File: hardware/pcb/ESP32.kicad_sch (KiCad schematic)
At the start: 8 parts, among them SW1 BOOT, U1 ESP32-WROOM-32

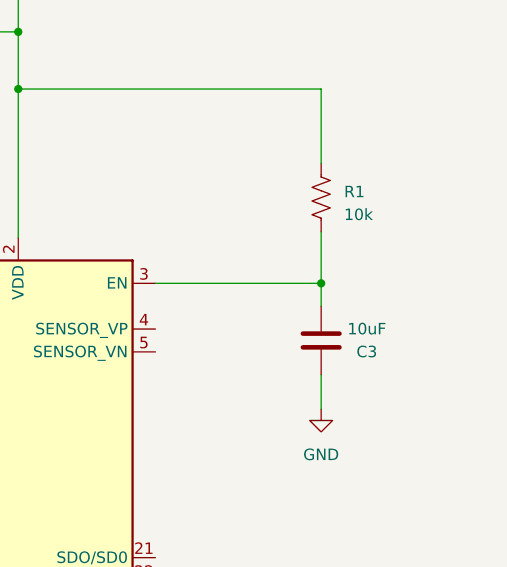
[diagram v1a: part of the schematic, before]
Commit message: Break out ESP enable pin
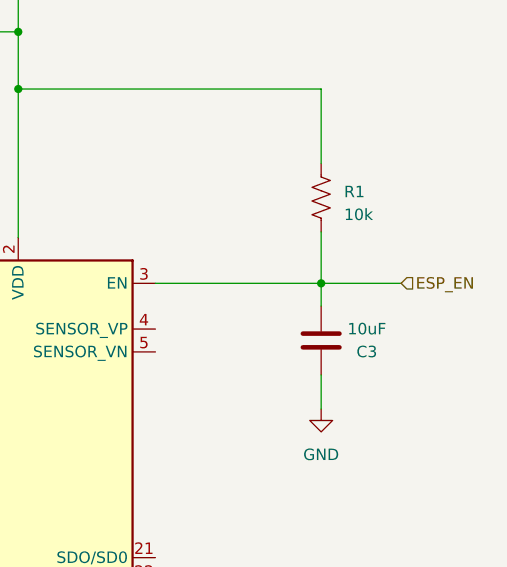
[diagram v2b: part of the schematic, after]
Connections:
- net ESP_EN: now reaches C3.2, R1.1, U1.3 (EN)
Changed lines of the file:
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@@
+    (stroke (width 0) (type default))
+  )
+  (wire (pts (xy 188.595 70.485) (xy 197.485 70.485))
     (stroke (width 0) (type default))
   )
@@
     (effects (font (size 1.27 1.27)) (justify right))
   )
+  (hierarchical_label "ESP_EN" (shape input) (at 197.485 70.485 0) (fields_autoplaced)
+    (effects (font (size 1.27 1.27)) (justify left))
+  )
   (hierarchical_label "ESP_TX" (shape input) (at 121.92 73.025 180) (fields_autoplaced)

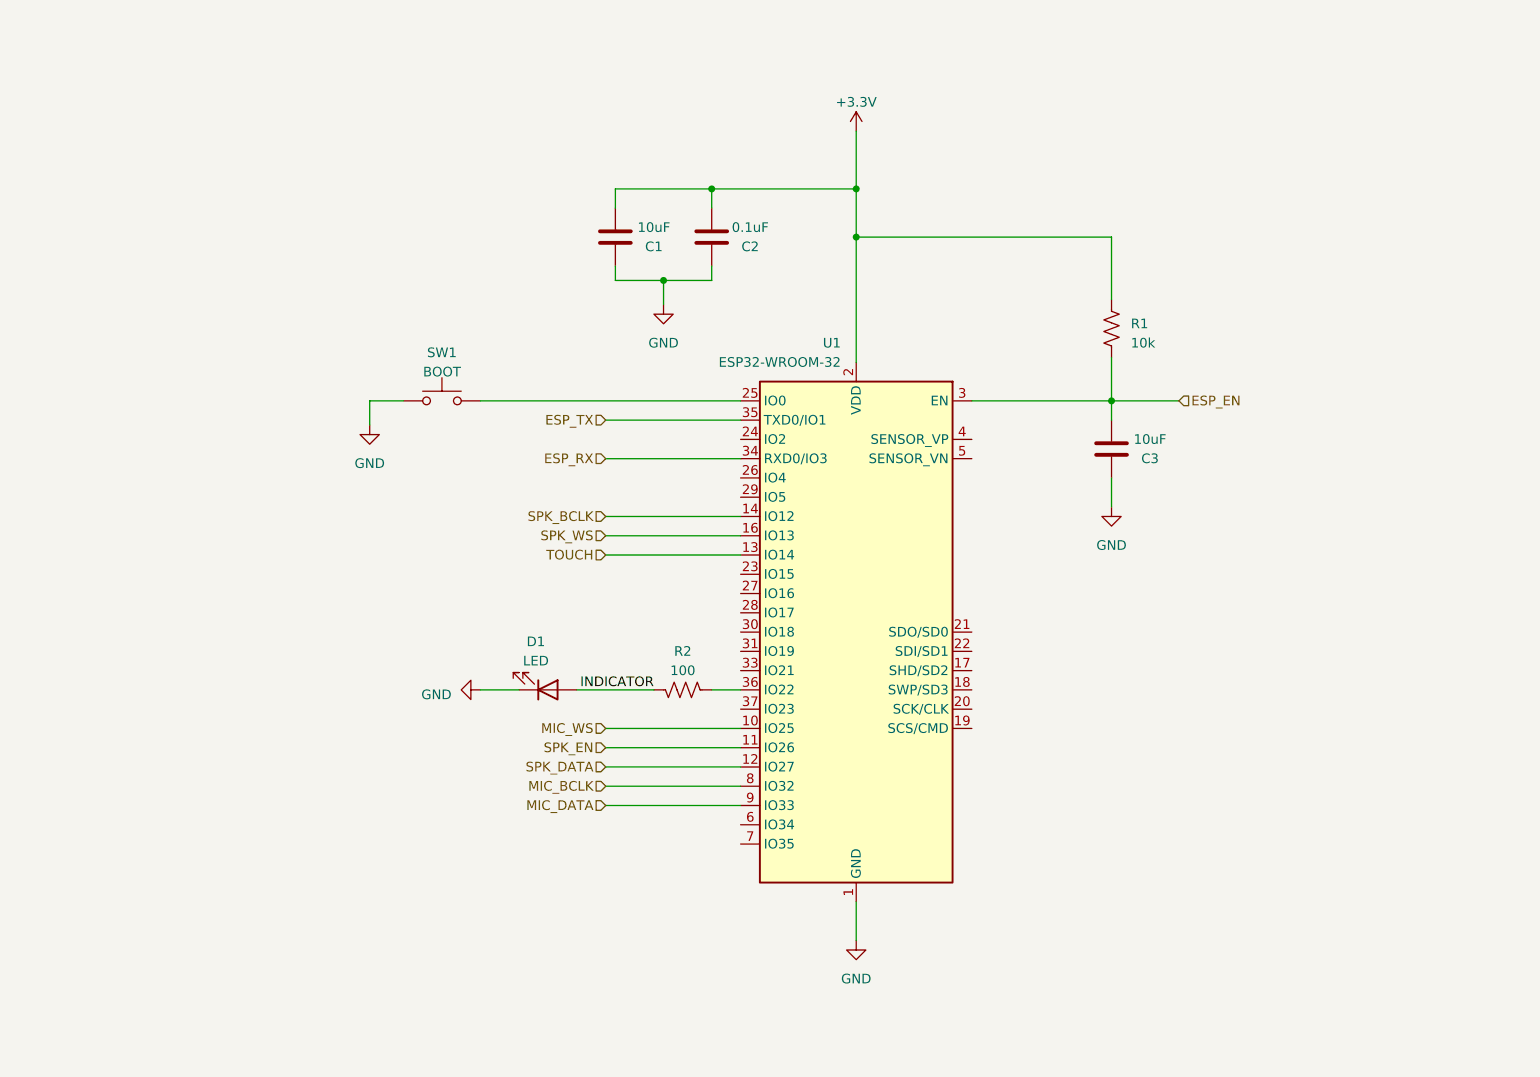
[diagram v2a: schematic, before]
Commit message: Replace ESP32 with ESP32-S3
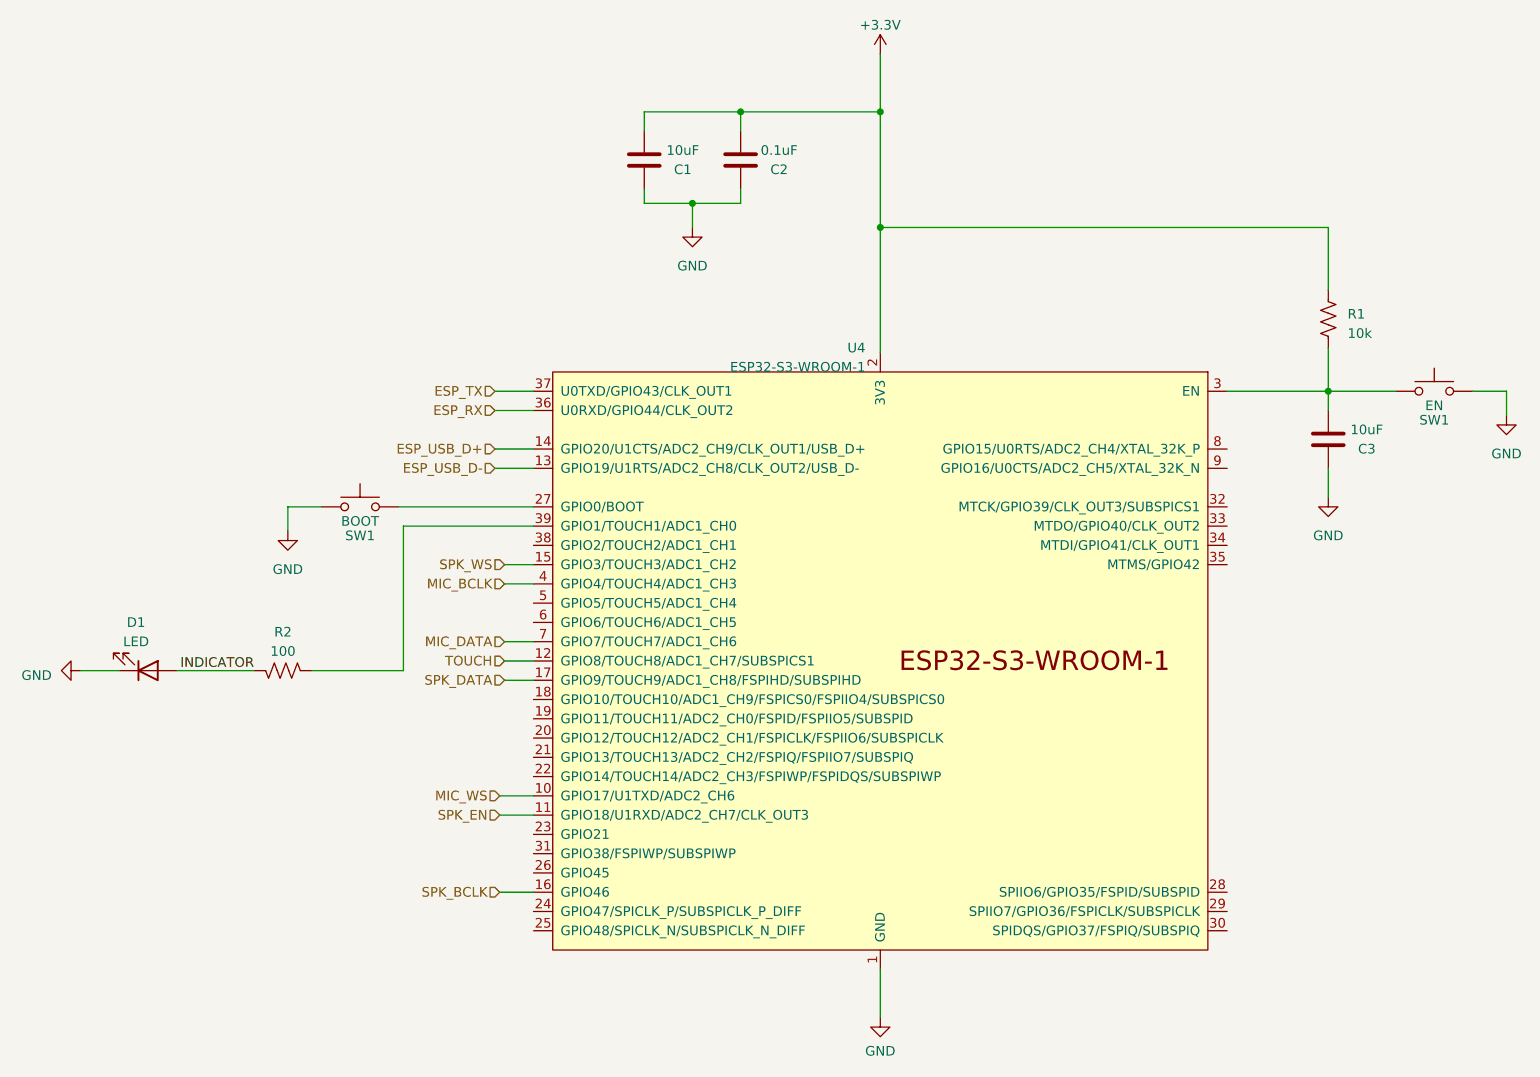
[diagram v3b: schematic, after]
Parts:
- removed SW1: BOOT, Button_Switch_SMD:SW_SPST_CK_RS282G05A3, symbol Switch:SW_Push
- removed U1: ESP32-WROOM-32, RF_Module:ESP32-WROOM-32, symbol RF_Module:ESP32-WROOM-32
- added SW1: BOOT, Button_Switch_SMD:SW_SPST_CK_RS282G05A3, symbol Switch:SW_Push
- added SW1: EN, Button_Switch_SMD:SW_SPST_CK_RS282G05A3, symbol Switch:SW_Push
- added U4: ESP32-S3-WROOM-1, Espressif:ESP32-S3-WROOM-1, symbol Espressif:ESP32-S3-WROOM-1
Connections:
- net +3.3V: now also U4.2 (3V3)
- net ESP_RX: now also U4.36 (U0RXD/GPIO44/CLK_OUT2)
- net ESP_TX: now also U4.37 (U0TXD/GPIO43/CLK_OUT1)
- net GND: now also SW1.1, SW1.1, U4.1 (GND), U4.40 (GND), U4.41 (GND)
- net MIC_BCLK: now also U4.4 (GPIO4/TOUCH4/ADC1_CH3)
- net MIC_DATA: now also U4.7 (GPIO7/TOUCH7/ADC1_CH6)
- net MIC_WS: now also U4.10 (GPIO17/U1TXD/ADC2_CH6)
- net SPK_BCLK: now also U4.16 (GPIO46)
- net SPK_DATA: now also U4.17 (GPIO9/TOUCH9/ADC1_CH8/FSPIHD/SUBSPIHD)
- net SPK_EN: now also U4.11 (GPIO18/U1RXD/ADC2_CH7/CLK_OUT3)
- net SPK_WS: now also U4.15 (GPIO3/TOUCH3/ADC1_CH2)
- net TOUCH: now also U4.12 (GPIO8/TOUCH8/ADC1_CH7/SUBSPICS1)
- net at R2.1: now also U4.39 (GPIO1/TOUCH1/ADC1_CH0)
- net ESP_EN: no longer names the net of C3.2, R1.1
- net ESP_EN: now also SW1.2, U4.3 (EN)
- new net: SW1.2, U4.27 (GPIO0/BOOT)
- new net ESP_USB_D+: U4.14 (GPIO20/U1CTS/ADC2_CH9/CLK_OUT1/USB_D+)
- new net ESP_USB_D-: U4.13 (GPIO19/U1RTS/ADC2_CH8/CLK_OUT2/USB_D-)

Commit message: Miscellaneous cleanup
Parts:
- R2: value 100 -> 150
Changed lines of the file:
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@@
   (symbol (lib_id "Device:R_US") (at 79.375 106.045 270) (mirror x) (unit 1)
     (in_bom yes) (on_board yes) (dnp no) (fields_autoplaced)
-    (property "Reference" "R2" (at 79.375 100.965 90)
+    (property "Reference" "R2" (at 79.375 101.6 90)
       (effects (font (size 1.27 1.27)))
     )
-    (property "Value" "100" (at 79.375 103.505 90)
+    (property "Value" "150" (at 79.375 104.14 90)
       (effects (font (size 1.27 1.27)))
     )

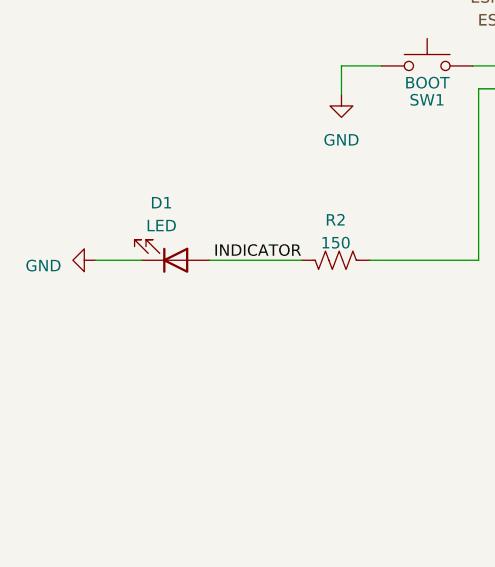
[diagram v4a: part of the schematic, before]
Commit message: Power speaker amplifier directly from battery
Also increase power trace widths
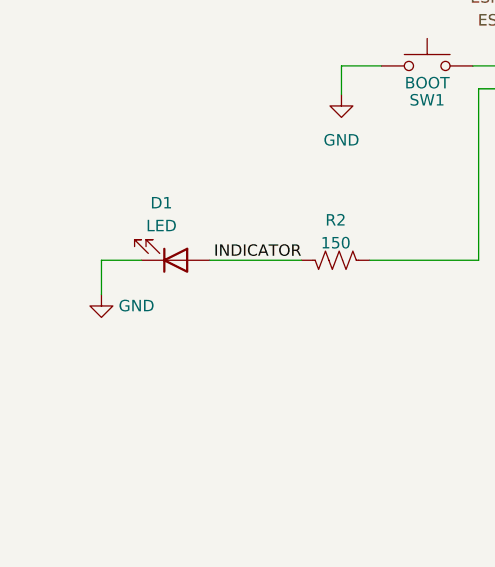
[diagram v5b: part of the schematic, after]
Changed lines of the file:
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@@
+    (stroke (width 0) (type default))
+  )
+  (wire (pts (xy 53.34 106.045) (xy 57.785 106.045))
     (stroke (width 0) (type default))
   )
@@
     (stroke (width 0) (type default))
   )
+  (wire (pts (xy 53.34 109.855) (xy 53.34 106.045))
+    (stroke (width 0) (type default))
+  )
   (wire (pts (xy 108.585 107.315) (xy 112.395 107.315))
     (stroke (width 0) (type default))
@@
   )
   (wire (pts (xy 203.835 69.215) (xy 217.17 69.215))
-    (stroke (width 0) (type default))
-  )
-  (wire (pts (xy 57.785 106.045) (xy 52.705 106.045))
     (stroke (width 0) (type default))
   )
@@
     )
   )
-  (symbol (lib_name "GND_1") (lib_id "power:GND") (at 52.705 106.045 270) (mirror x) (unit 1)
-    (in_bom yes) (on_board yes) (dnp no) (fields_autoplaced)
-    (property "Reference" "#PWR05" (at 46.355 106.045 0)
-      (effects (font (size 1.27 1.27)) hide)
-    )
-    (property "Value" "GND" (at 48.895 106.68 90)
+  (symbol (lib_name "GND_1") (lib_id "power:GND") (at 53.34 109.855 0) (mirror y) (unit 1)
+    (in_bom yes) (on_board yes) (dnp no) (fields_autoplaced)
+    (property "Reference" "#PWR05" (at 53.34 116.205 0)
+      (effects (font (size 1.27 1.27)) hide)
+    )
+    (property "Value" "GND" (at 55.245 111.125 0)
       (effects (font (size 1.27 1.27)) (justify right))
     )
-    (property "Footprint" "" (at 52.705 106.045 0)
-      (effects (font (size 1.27 1.27)) hide)
-    )
-    (property "Datasheet" "" (at 52.705 106.045 0)
-      (effects (font (size 1.27 1.27)) hide)
-    )
+    (property "Footprint" "" (at 53.34 109.855 0)
+      (effects (font (size 1.27 1.27)) hide)
+    )
+    (property "Datasheet" "" (at 53.34 109.855 0)
+      (effects (font (size 1.27 1.27)) hide)
+    )

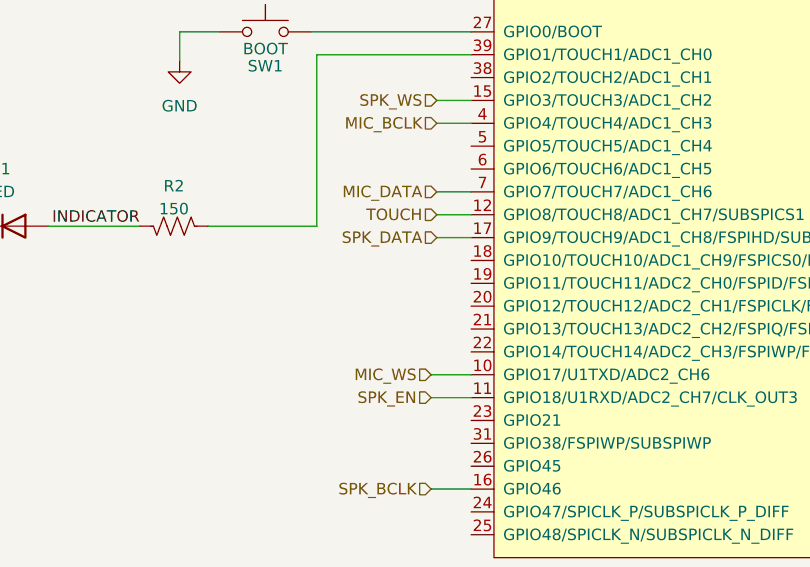
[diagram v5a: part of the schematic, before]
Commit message: Add extra touch pads
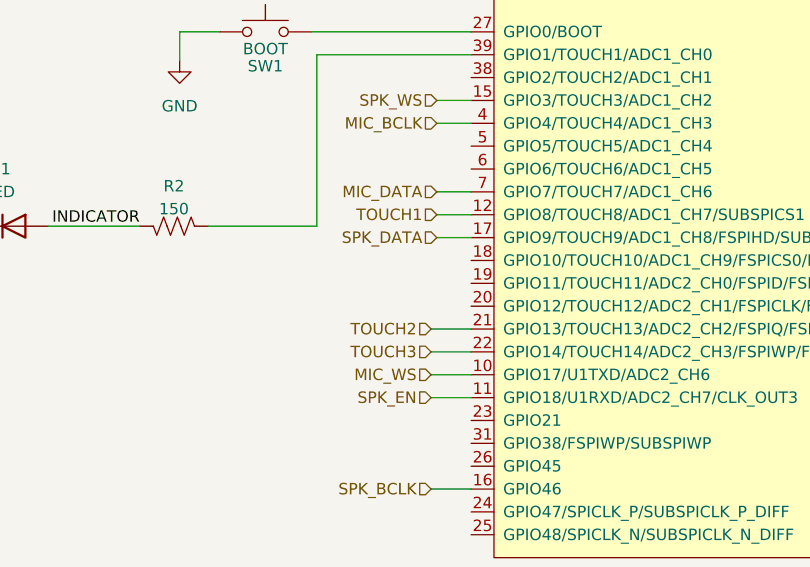
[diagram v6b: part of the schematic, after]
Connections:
- net TOUCH2: now reaches U4.21 (GPIO13/TOUCH13/ADC2_CH2/FSPIQ/FSPIIO7/SUBSPIQ)
- net TOUCH3: now reaches U4.22 (GPIO14/TOUCH14/ADC2_CH3/FSPIWP/FSPIDQS/SUBSPIWP)
- net TOUCH renamed TOUCH1
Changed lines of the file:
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@@
+    (stroke (width 0) (type default))
+  )
+  (wire (pts (xy 107.95 117.475) (xy 112.395 117.475))
     (stroke (width 0) (type default))
   )
@@
     (stroke (width 0) (type default))
   )
+  (wire (pts (xy 107.95 120.015) (xy 112.395 120.015))
+    (stroke (width 0) (type default))
+  )
   (wire (pts (xy 203.835 69.215) (xy 217.17 69.215))
     (stroke (width 0) (type default))
@@
     (effects (font (size 1.27 1.27)) (justify right))
   )
-  (hierarchical_label "TOUCH" (shape input) (at 108.585 104.775 180) (fields_autoplaced)
+  (hierarchical_label "TOUCH1" (shape input) (at 108.585 104.775 180) (fields_autoplaced)
     (effects (font (size 1.27 1.27)) (justify right))
   )
   (hierarchical_label "ESP_USB_D-" (shape input) (at 107.315 79.375 180) (fields_autoplaced)
+    (effects (font (size 1.27 1.27)) (justify right))
+  )
+  (hierarchical_label "TOUCH3" (shape input) (at 107.95 120.015 180) (fields_autoplaced)
     (effects (font (size 1.27 1.27)) (justify right))
   )
@@
     (effects (font (size 1.27 1.27)) (justify right))
   )
+  (hierarchical_label "TOUCH2" (shape input) (at 107.95 117.475 180) (fields_autoplaced)
+    (effects (font (size 1.27 1.27)) (justify right))
+  )
